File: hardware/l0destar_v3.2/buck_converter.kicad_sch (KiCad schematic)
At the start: 11 parts

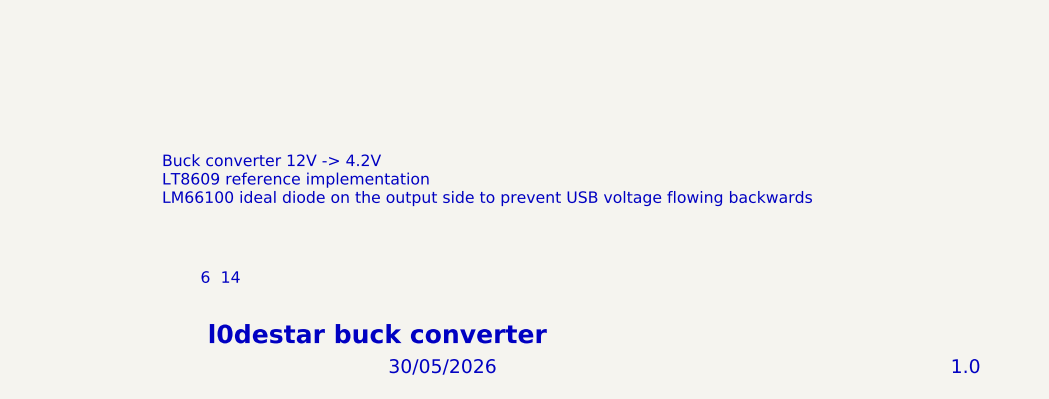
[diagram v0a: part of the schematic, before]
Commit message: update sheet annotations
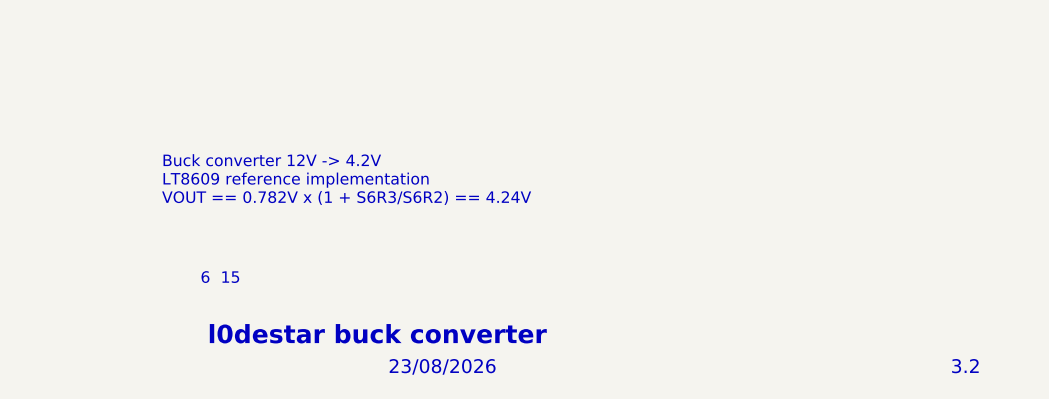
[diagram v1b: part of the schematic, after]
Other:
- note added: "15"
- note added: "23/08/2026"
- note added: "3.2"
- note added: "Buck converter 12V -> 4.2V LT8609 reference implementation VOUT == 0.782V x (1 + S6R3/S6R2) == 4.24V"
- note removed: "1.0"
- note removed: "14"
- note removed: "30/05/2026"
- note removed: "Buck converter 12V -> 4.2V LT8609 reference implementation LM66100 ideal diode on the output side to prevent USB voltage flowing backwards"
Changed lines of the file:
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@@
 	(generator_version "10.0")
 	(paper "A4")
-	(text "30/05/2026"
+	(text "23/08/2026"
 		(exclude_from_sim no)
 		(at 205.994 193.294 0)
@@
 		)
 	)
-	(text "14"
+	(text "15"
 		(exclude_from_sim no)
 		(at 188.468 183.388 0)
@@
 		)
 	)
-	(text "Buck converter 12V -> 4.2V\nLT8609 reference implementation\nLM66100 ideal diode on the output side to prevent USB voltage flowing backwards"
+	(text "Buck converter 12V -> 4.2V\nLT8609 reference implementation\nVOUT == 0.782V x (1 + S6R3/S6R2) == 4.24V"
 		(exclude_from_sim no)
 		(at 180.848 172.466 0)
@@
 		)
 	)
-	(text "1.0"
+	(text "3.2"
 		(exclude_from_sim no)
 		(at 268.478 193.294 0)

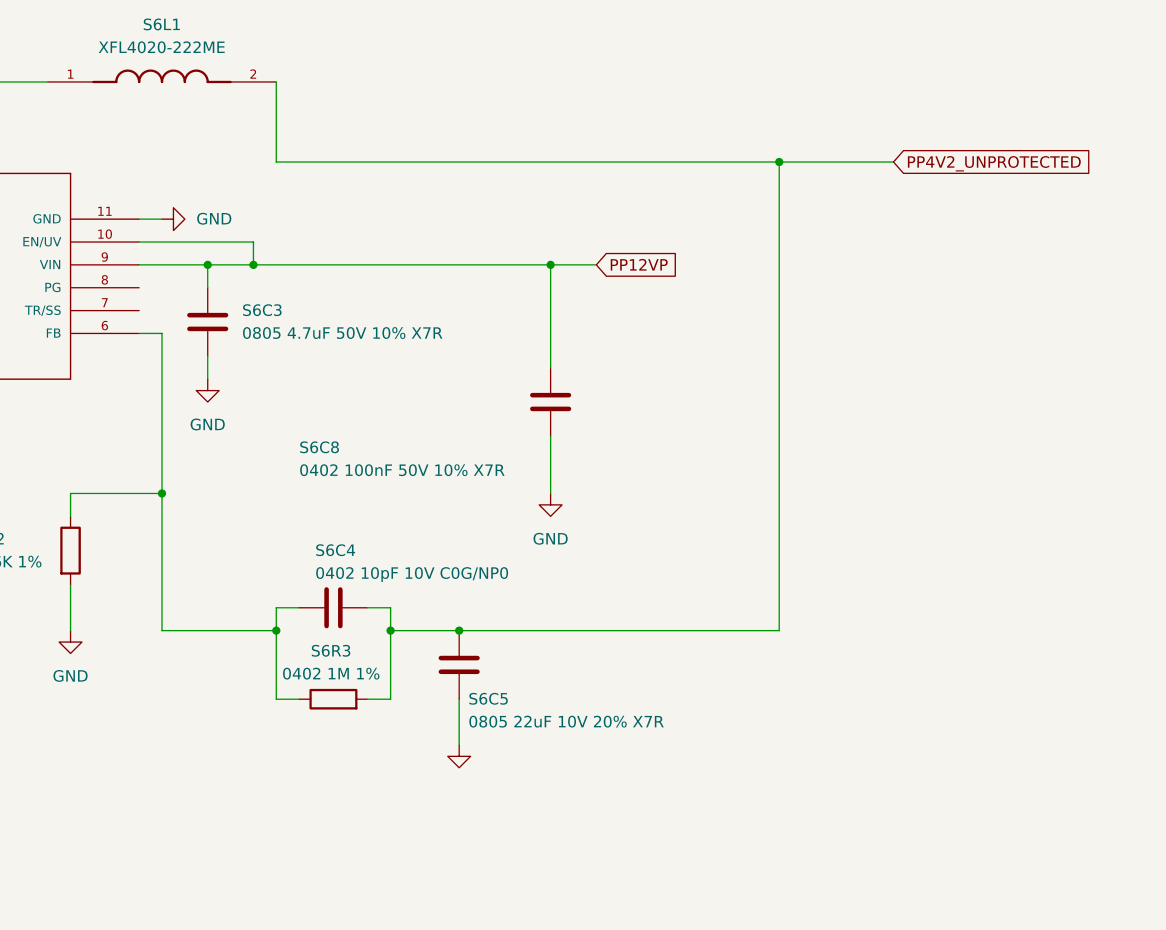
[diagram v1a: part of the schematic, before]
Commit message: spec anti-sulfur for S6R3
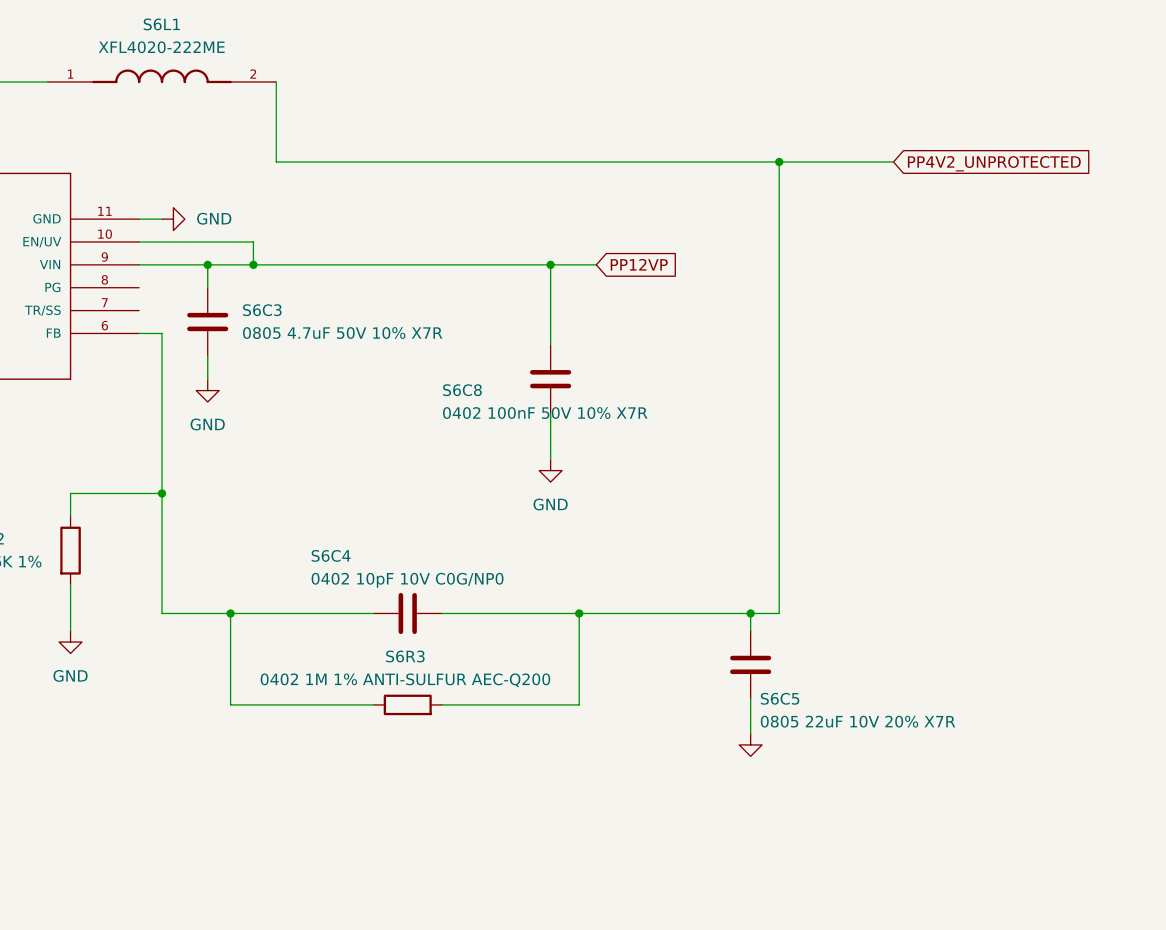
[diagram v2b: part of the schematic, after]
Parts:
- S6R3: value 0402 1M 1% -> 0402 1M 1% ANTI-SULFUR AEC-Q200
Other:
- moved on the sheet: S6C4, S6C5, S6C8, S6R3

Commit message: schematic<>readme discrepency fixes
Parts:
- S6C1: value 0402 100nF 25V 10% X7R -> 0402 100nF 50V 10% X7R; Manufacturer_Name Multicomp Pro -> Murata; Manufacturer_Part_Number MC0402B104K250CT -> GRM155R71H104KE14D
- S6C4: value 0402 10pF 10V C0G/NP0 -> 0402 10pF 50V C0G/NP0
- S6C8: Manufacturer_Name Taiyo Yuden -> Murata; Manufacturer_Part_Number MCASU105SB7104KFNA01 -> GRM155R71H104KE14D
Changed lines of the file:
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@@
 			)
 		)
-		(property "Value" "0402 100nF 25V 10% X7R"
+		(property "Value" "0402 100nF 50V 10% X7R"
 			(at 28.956 43.434 0)
 			(show_name no)
@@
 			)
 		)
-		(property "Datasheet" "https://uk.farnell.com/multicomp-pro/mc0402b104k250ct/cap-0-1-f-25v-10-x7r-0402/dp/2320759"
+		(property "Datasheet" ""
 			(at 25.4 41.91 0)
 			(hide yes)
@@
 			)
 		)
-		(property "Description" "Unpolarized capacitor"
+		(property "Description" ""
 			(at 25.4 41.91 0)
 			(hide yes)
@@
 			)
 		)
-		(property "Manufacturer_Part_Number" "MC0402B104K250CT"
+		(property "Manufacturer_Part_Number" "GRM155R71H104KE14D"
 			(at 25.4 41.91 0)
 			(hide yes)
@@
 			)
 		)
-		(property "Manufacturer_Name" "Multicomp Pro"
+		(property "Manufacturer_Name" "Murata"
 			(at 25.4 41.91 0)
 			(hide yes)
@@
 			)
 		)
-		(property "Datasheet" "https://ds.yuden.co.jp/TYCOMPAS/or/detail?pn=MCASU105SB7104KFNA01&u=M"
+		(property "Datasheet" ""
 			(at 167.64 60.96 0)
 			(hide yes)
@@
 			)
 		)
-		(property "Description" "Unpolarized capacitor"
+		(property "Description" ""
 			(at 167.64 60.96 0)
 			(hide yes)
@@
 			)
 		)
-		(property "Manufacturer_Part_Number" "MCASU105SB7104KFNA01"
+		(property "Manufacturer_Part_Number" "GRM155R71H104KE14D"
 			(at 167.64 60.96 0)
 			(hide yes)
@@
 			)
 		)
-		(property "Manufacturer_Name" "Taiyo Yuden"
+		(property "Manufacturer_Name" "Murata"
 			(at 167.64 60.96 0)
 			(hide yes)
@@
 			)
 		)
-		(property "Value" "0402 10pF 10V C0G/NP0"
+		(property "Value" "0402 10pF 50V C0G/NP0"
 			(at 140.97 83.185 90)
 			(show_name no)
